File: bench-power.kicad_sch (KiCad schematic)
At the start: 32 parts, among them J1 PWR_OUT, J2 POWER_IN_BRD, J3 LOAD, J4 POWER_IN

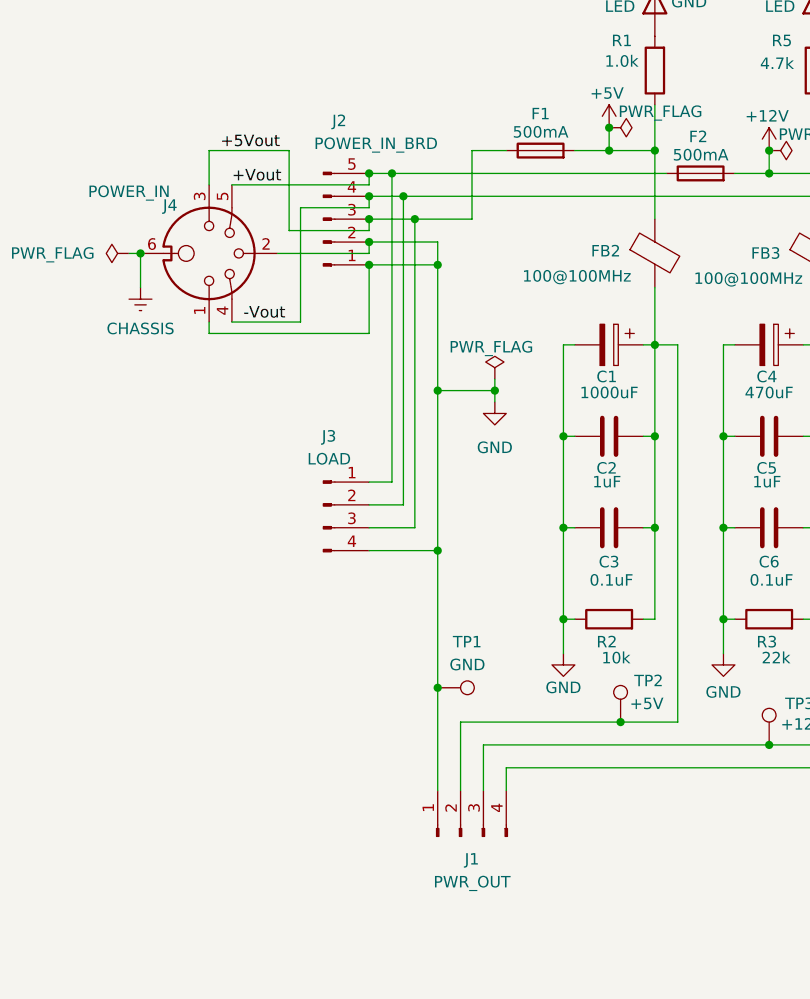
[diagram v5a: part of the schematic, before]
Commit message: shuffle jst connectors
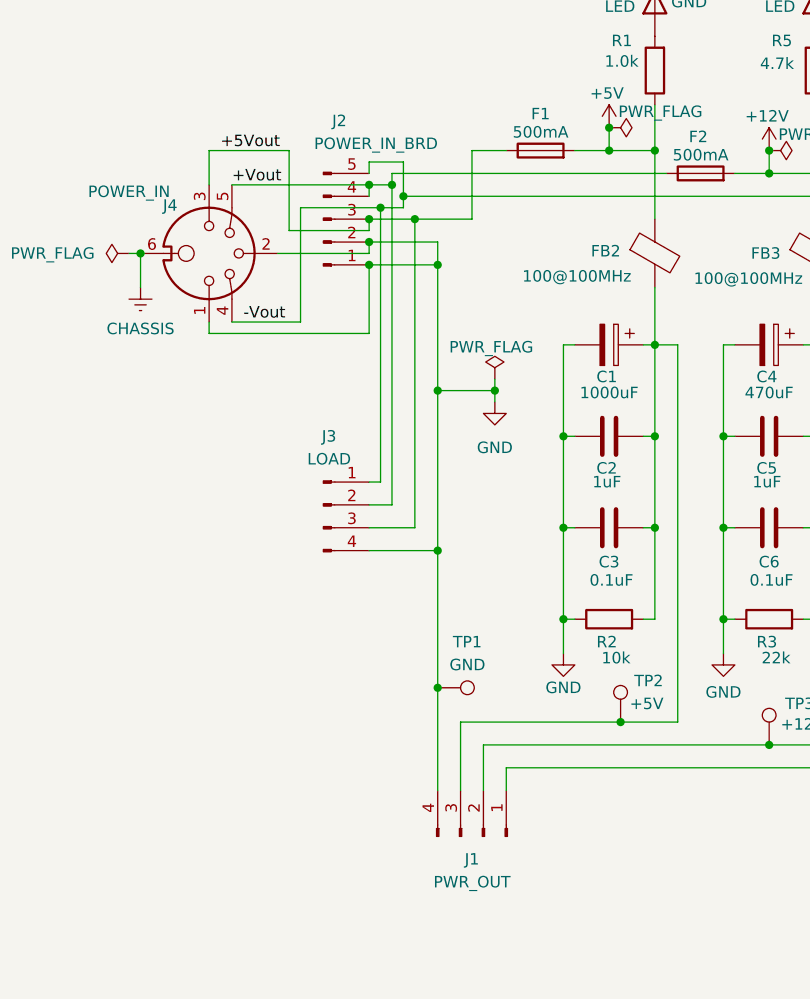
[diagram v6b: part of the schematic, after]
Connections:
- net +Vout: now also J2.4 (Pin_4), J3.2 (Pin_2); no longer J2.5 (Pin_5), J3.1 (Pin_1)
- net -Vout: now also J2.5 (Pin_5), J3.1 (Pin_1); no longer J2.4 (Pin_4), J3.2 (Pin_2)
- net GND: now also J1.4 (Pin_4); no longer J1.1 (Pin_1)
- net at C1.1, C2.2, C3.2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: now also J1.3 (Pin_3); no longer J1.2 (Pin_2)
- net at C7.2, C8.2, C9.2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: now also J1.1 (Pin_1); no longer J1.4 (Pin_4)
- net at C4.1, C5.2, C6.2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: now also J1.2 (Pin_2); no longer J1.3 (Pin_3)
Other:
- moved on the sheet: J1
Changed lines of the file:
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@@
 	)
 	(junction
-		(at 55.88 64.77)
-		(diameter 0)
-		(color 0 0 0 0)
-	)
-	(junction
-		(at 63.5 121.92)
-		(diameter 0)
-		(color 0 0 0 0)
-	)
-	(junction
 		(at 100.33 128.27)
 		(diameter 0)
@@
 	)
 	(junction
-		(at 59.69 67.31)
+		(at 82.55 59.69)
 		(diameter 0)
 		(color 0 0 0 0)
 	)
 	(junction
-		(at 82.55 59.69)
+		(at 123.19 104.14)
 		(diameter 0)
 		(color 0 0 0 0)
 	)
 	(junction
-		(at 123.19 104.14)
+		(at 118.11 64.77)
 		(diameter 0)
 		(color 0 0 0 0)
 	)
 	(junction
-		(at 118.11 64.77)
+		(at 57.15 68.58)
 		(diameter 0)
 		(color 0 0 0 0)
@@
 	)
 	(junction
+		(at 59.69 67.31)
+		(diameter 0)
+		(color 0 0 0 0)
+	)
+	(junction
 		(at 77.47 93.98)
 		(diameter 0)
@@
 	)
 	(junction
+		(at 55.88 66.04)
+		(diameter 0)
+		(color 0 0 0 0)
+	)
+	(junction
 		(at 113.03 104.14)
 		(diameter 0)
@@
 	)
 	(junction
-		(at 63.5 74.93)
+		(at 58.42 66.04)
 		(diameter 0)
 		(color 0 0 0 0)
 	)
 	(junction
-		(at 113.03 114.3)
+		(at 63.5 74.93)
 		(diameter 0)
 		(color 0 0 0 0)
 	)
 	(junction
-		(at 58.42 64.77)
+		(at 63.5 121.92)
 		(diameter 0)
 		(color 0 0 0 0)
 	)
 	(junction
-		(at 87.63 93.98)
+		(at 113.03 114.3)
 		(diameter 0)
 		(color 0 0 0 0)
 	)
 	(junction
-		(at 55.88 67.31)
+		(at 87.63 93.98)
 		(diameter 0)
 		(color 0 0 0 0)
@@
 	(wire
 		(pts
-			(xy 63.5 88.9) (xy 63.5 106.68)
+			(xy 63.5 121.92) (xy 63.5 133.35)
 		)
 		(stroke
@@
 	(wire
 		(pts
-			(xy 55.88 64.77) (xy 58.42 64.77)
+			(xy 63.5 88.9) (xy 63.5 106.68)
 		)
 		(stroke
@@
 	(wire
 		(pts
+			(xy 55.88 64.77) (xy 55.88 63.5)
+		)
+		(stroke
+			(width 0)
+			(type default)
+		)
+	)
+	(wire
+		(pts
 			(xy 87.63 83.82) (xy 87.63 93.98)
 		)
@@
 	(wire
 		(pts
-			(xy 55.88 68.58) (xy 55.88 67.31)
+			(xy 104.14 104.14) (xy 105.41 104.14)
 		)
 		(stroke
@@
 	(wire
 		(pts
-			(xy 104.14 104.14) (xy 105.41 104.14)
+			(xy 95.25 104.14) (xy 95.25 114.3)
 		)
 		(stroke
@@
 	(wire
 		(pts
-			(xy 95.25 104.14) (xy 95.25 114.3)
+			(xy 59.69 68.58) (xy 59.69 67.31)
 		)
 		(stroke
@@
 	(wire
 		(pts
-			(xy 58.42 99.06) (xy 58.42 64.77)
+			(xy 55.88 66.04) (xy 58.42 66.04)
 		)
 		(stroke
@@
 	(wire
 		(pts
-			(xy 59.69 101.6) (xy 59.69 67.31)
+			(xy 48.26 68.58) (xy 57.15 68.58)
 		)
 		(stroke
@@
 	(wire
 		(pts
-			(xy 48.26 68.58) (xy 55.88 68.58)
+			(xy 55.88 101.6) (xy 58.42 101.6)
 		)
 		(stroke
@@
 	(wire
 		(pts
-			(xy 66.04 125.73) (xy 66.04 133.35)
-		)
-		(stroke
-			(width 0)
-			(type default)
-		)
-	)
-	(wire
-		(pts
 			(xy 87.63 104.14) (xy 87.63 114.3)
 		)
@@
 	(wire
 		(pts
-			(xy 68.58 128.27) (xy 68.58 133.35)
+			(xy 105.41 57.15) (xy 105.41 64.77)
 		)
 		(stroke
@@
 	(wire
 		(pts
-			(xy 105.41 57.15) (xy 105.41 64.77)
+			(xy 57.15 68.58) (xy 59.69 68.58)
 		)
 		(stroke
@@
 	(wire
 		(pts
-			(xy 30.48 73.66) (xy 30.48 77.47)
+			(xy 58.42 66.04) (xy 58.42 64.77)
 		)
 		(stroke
@@
 	(wire
 		(pts
-			(xy 105.41 77.47) (xy 105.41 83.82)
+			(xy 30.48 73.66) (xy 30.48 77.47)
 		)
 		(stroke
@@
 	(wire
 		(pts
-			(xy 95.25 104.14) (xy 96.52 104.14)
+			(xy 105.41 77.47) (xy 105.41 83.82)
 		)
 		(stroke
@@
 	(wire
 		(pts
-			(xy 121.92 104.14) (xy 123.19 104.14)
+			(xy 95.25 104.14) (xy 96.52 104.14)
 		)
 		(stroke
@@
 	(wire
 		(pts
-			(xy 55.88 67.31) (xy 59.69 67.31)
+			(xy 121.92 104.14) (xy 123.19 104.14)
 		)
 		(stroke
@@
 	(wire
 		(pts
-			(xy 55.88 99.06) (xy 58.42 99.06)
+			(xy 118.11 67.31) (xy 123.19 67.31)
 		)
 		(stroke
@@
 	(wire
 		(pts
-			(xy 118.11 67.31) (xy 123.19 67.31)
+			(xy 121.92 83.82) (xy 123.19 83.82)
 		)
 		(stroke
@@
 	(wire
 		(pts
-			(xy 121.92 83.82) (xy 123.19 83.82)
+			(xy 114.3 67.31) (xy 118.11 67.31)
 		)
 		(stroke
@@
 	(wire
 		(pts
-			(xy 114.3 67.31) (xy 118.11 67.31)
+			(xy 87.63 62.23) (xy 87.63 69.85)
 		)
 		(stroke
@@
 	(wire
 		(pts
-			(xy 87.63 62.23) (xy 87.63 69.85)
+			(xy 95.25 83.82) (xy 95.25 93.98)
 		)
 		(stroke
@@
 	(wire
 		(pts
-			(xy 95.25 83.82) (xy 95.25 93.98)
+			(xy 90.17 83.82) (xy 90.17 125.73)
 		)
 		(stroke
@@
 	(wire
 		(pts
-			(xy 90.17 83.82) (xy 90.17 125.73)
+			(xy 55.88 104.14) (xy 60.96 104.14)
 		)
 		(stroke
@@
 	(wire
 		(pts
-			(xy 55.88 104.14) (xy 60.96 104.14)
+			(xy 71.12 130.81) (xy 71.12 133.35)
 		)
 		(stroke
@@
 	(wire
 		(pts
+			(xy 55.88 99.06) (xy 57.15 99.06)
+		)
+		(stroke
+			(width 0)
+			(type default)
+		)
+	)
+	(wire
+		(pts
 			(xy 38.1 81.28) (xy 38.1 82.55)
 		)
@@
 	(wire
 		(pts
+			(xy 57.15 68.58) (xy 57.15 99.06)
+		)
+		(stroke
+			(width 0)
+			(type default)
+		)
+	)
+	(wire
+		(pts
 			(xy 63.5 106.68) (xy 63.5 121.92)
 		)
@@
 	(wire
 		(pts
-			(xy 71.12 130.81) (xy 71.12 133.35)
+			(xy 55.88 63.5) (xy 59.69 63.5)
+		)
+		(stroke
+			(width 0)
+			(type default)
+		)
+	)
+	(wire
+		(pts
+			(xy 66.04 125.73) (xy 66.04 133.35)
 		)
 		(stroke
@@
 	(wire
 		(pts
+			(xy 55.88 67.31) (xy 55.88 66.04)
+		)
+		(stroke
+			(width 0)
+			(type default)
+		)
+	)
+	(wire
+		(pts
 			(xy 123.19 83.82) (xy 125.73 83.82)
 		)
@@
 	(wire
 		(pts
-			(xy 55.88 101.6) (xy 59.69 101.6)
+			(xy 96.52 64.77) (xy 100.33 64.77)
 		)
 		(stroke
@@
 	(wire
 		(pts
-			(xy 96.52 64.77) (xy 100.33 64.77)
+			(xy 58.42 66.04) (xy 58.42 101.6)
 		)
 		(stroke
@@
 	(wire
 		(pts
-			(xy 30.48 73.66) (xy 29.21 73.66)
+			(xy 59.69 63.5) (xy 59.69 67.31)
 		)
 		(stroke
@@
 	(wire
 		(pts
-			(xy 113.03 93.98) (xy 114.3 93.98)
+			(xy 30.48 73.66) (xy 29.21 73.66)
 		)
 		(stroke
@@
 	(wire
 		(pts
-			(xy 77.47 83.82) (xy 78.74 83.82)
+			(xy 113.03 93.98) (xy 114.3 93.98)
 		)
 		(stroke
@@
 	(wire
 		(pts
-			(xy 55.88 66.04) (xy 55.88 64.77)
+			(xy 77.47 83.82) (xy 78.74 83.82)
 		)
 		(stroke
@@
 	(wire
 		(pts
-			(xy 63.5 121.92) (xy 63.5 133.35)
+			(xy 82.55 59.69) (xy 82.55 62.23)
 		)
 		(stroke
@@
 	(wire
 		(pts
-			(xy 82.55 59.69) (xy 82.55 62.23)
+			(xy 60.96 69.85) (xy 67.31 69.85)
 		)
 		(stroke
@@
 	(wire
 		(pts
-			(xy 60.96 69.85) (xy 67.31 69.85)
+			(xy 63.5 72.39) (xy 63.5 74.93)
 		)
 		(stroke
@@
 	(wire
 		(pts
-			(xy 63.5 72.39) (xy 63.5 74.93)
+			(xy 105.41 83.82) (xy 107.95 83.82)
 		)
 		(stroke
@@
 	(wire
 		(pts
-			(xy 105.41 83.82) (xy 107.95 83.82)
+			(xy 113.03 83.82) (xy 113.03 93.98)
 		)
 		(stroke
@@
 	(wire
 		(pts
-			(xy 113.03 83.82) (xy 113.03 93.98)
+			(xy 68.58 128.27) (xy 68.58 133.35)
 		)
 		(stroke
@@
 	(symbol
 		(lib_id "Connector:Conn_01x04_Pin")
-		(at 66.04 138.43 90)
+		(at 68.58 138.43 270)
+		(mirror x)
 		(unit 1)
 		(exclude_from_sim no)
@@
 		(on_board yes)
 		(dnp no)
-		(fields_autoplaced yes)
 		(property "Reference" "J1"
 			(at 67.31 140.97 90)
@@
 		)
 		(property "Footprint" "Connector_JST:JST_XH_B4B-XH-A_1x04_P2.50mm_Vertical"
-			(at 66.04 138.43 0)
+			(at 68.58 138.43 0)
 			(effects
 				(font
@@
 		)
 		(property "Datasheet" "~"
-			(at 66.04 138.43 0)
+			(at 68.58 138.43 0)
 			(effects
 				(font
@@
 		)
 		(property "Description" "Generic connector, single row, 01x04, script generated"
-			(at 66.04 138.43 0)
+			(at 68.58 138.43 0)
 			(effects
 				(font
